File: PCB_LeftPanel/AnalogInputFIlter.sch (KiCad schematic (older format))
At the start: 24 parts, among them J24 Conn_01x03, J25 Conn_01x03, J26 Conn_01x03, J27 Conn_01x03, J28 Conn_01x03, J29 Conn_01x03, J30 Conn_01x03, J31 Conn_01x03

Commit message: Add files via upload
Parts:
- added J36: Conn_01x08_Male, Connector_PinHeader_2.54mm:PinHeader_1x08_P2.54mm_Vertical, symbol Connector:Conn_01x08_Male
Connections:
- net PA0: now also J36.1 (Pin_1)
- net PA1: now also J36.2 (Pin_2)
- net PA2: now also J36.3 (Pin_3)
- net PA3: now also J36.4 (Pin_4)
- net PA4: now also J36.5 (Pin_5)
- net PA5: now also J36.6 (Pin_6)
- net PA6: now also J36.7 (Pin_7)
- net PA7: now also J36.8 (Pin_8)
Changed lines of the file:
@@
 Wire Wire Line
 	6450 4700 6850 4700
+$Comp
+L Connector:Conn_01x08_Male J36
+U 1 1 616B3B5E
+P 2800 2000
+F 0 "J36" H 2908 2481 50  0000 C CNN
+F 1 "Conn_01x08_Male" H 2908 2390 50  0000 C CNN
+F 2 "Connector_PinHeader_2.54mm:PinHeader_1x08_P2.54mm_Vertical" H 2800 2000 50  0001 C CNN
+F 3 "~" H 2800 2000 50  0001 C CNN
+	1    2800 2000
+	1    0    0    -1
+$EndComp
+Wire Wire Line
+	3000 1700 5450 1700
+Connection ~ 5450 1700
+Wire Wire Line
+	3000 1800 4500 1800
+Wire Wire Line
+	4500 1800 4500 2200
+Wire Wire Line
+	4500 2200 5450 2200
+Connection ~ 5450 2200
+Wire Wire Line
+	3000 1900 4400 1900
+Wire Wire Line
+	4400 1900 4400 2700
+Wire Wire Line
+	4400 2700 5450 2700
+Connection ~ 5450 2700
+Wire Wire Line
+	3000 2000 4300 2000
+Wire Wire Line
+	4300 2000 4300 3200
+Wire Wire Line
+	4300 3200 5450 3200
+Connection ~ 5450 3200
+Wire Wire Line
+	5450 3700 4200 3700
+Wire Wire Line
+	4200 3700 4200 2100
+Wire Wire Line
+	4200 2100 3000 2100
+Connection ~ 5450 3700
+Wire Wire Line
+	3000 2200 4100 2200
+Wire Wire Line
+	4100 2200 4100 4200
+Wire Wire Line
+	4100 4200 5450 4200
+Connection ~ 5450 4200
+Wire Wire Line
+	5450 4700 4000 4700
+Wire Wire Line
+	4000 4700 4000 2300
+Wire Wire Line
+	4000 2300 3000 2300
+Connection ~ 5450 4700
+Wire Wire Line
+	3000 2400 3900 2400
+Wire Wire Line
+	3900 2400 3900 5200
+Wire Wire Line
+	3900 5200 5450 5200
+Connection ~ 5450 5200
 $EndSCHEMATC

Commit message: Add files via upload
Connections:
- net GND: now also C10.2, C11.2, C12.2, C13.2, C14.2, C15.2, C16.2, C3.2; no longer C10.1, C11.1, C12.1, C13.1, C14.1, C15.1, C16.1, C3.1
- net PA0: now also C3.1; no longer C3.2
- net PA1: now also C10.1; no longer C10.2
- net PA2: now also C11.1; no longer C11.2
- net PA3: now also C12.1; no longer C12.2
- net PA4: now also C13.1; no longer C13.2
- net PA5: now also C14.1; no longer C14.2
- net PA6: now also C15.1; no longer C15.2
- net PA7: now also C16.1; no longer C16.2
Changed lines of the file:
@@
 F 3 "~" H 6300 1700 50  0001 C CNN
 	1    6300 1700
-	0    1    1    0
+	0    -1   -1   0
 $EndComp
 $Comp
@@
 F 3 "~" H 6300 2200 50  0001 C CNN
 	1    6300 2200
-	0    1    1    0
+	0    -1   -1   0
 $EndComp
 $Comp
@@
 F 3 "~" H 6300 2700 50  0001 C CNN
 	1    6300 2700
-	0    1    1    0
+	0    -1   -1   0
 $EndComp
 $Comp
@@
 F 3 "~" H 6300 3200 50  0001 C CNN
 	1    6300 3200
-	0    1    1    0
+	0    -1   -1   0
 $EndComp
 $Comp
@@
 F 3 "~" H 6300 3700 50  0001 C CNN
 	1    6300 3700
-	0    1    1    0
+	0    -1   -1   0
 $EndComp
 $Comp
@@
 F 3 "~" H 6300 4200 50  0001 C CNN
 	1    6300 4200
-	0    1    1    0
+	0    -1   -1   0
 $EndComp
 $Comp
@@
 F 3 "~" H 6300 4700 50  0001 C CNN
 	1    6300 4700
-	0    1    1    0
+	0    -1   -1   0
 $EndComp
 $Comp
@@
 F 3 "~" H 6300 5200 50  0001 C CNN
 	1    6300 5200
-	0    1    1    0
+	0    -1   -1   0
 $EndComp
 Wire Wire Line

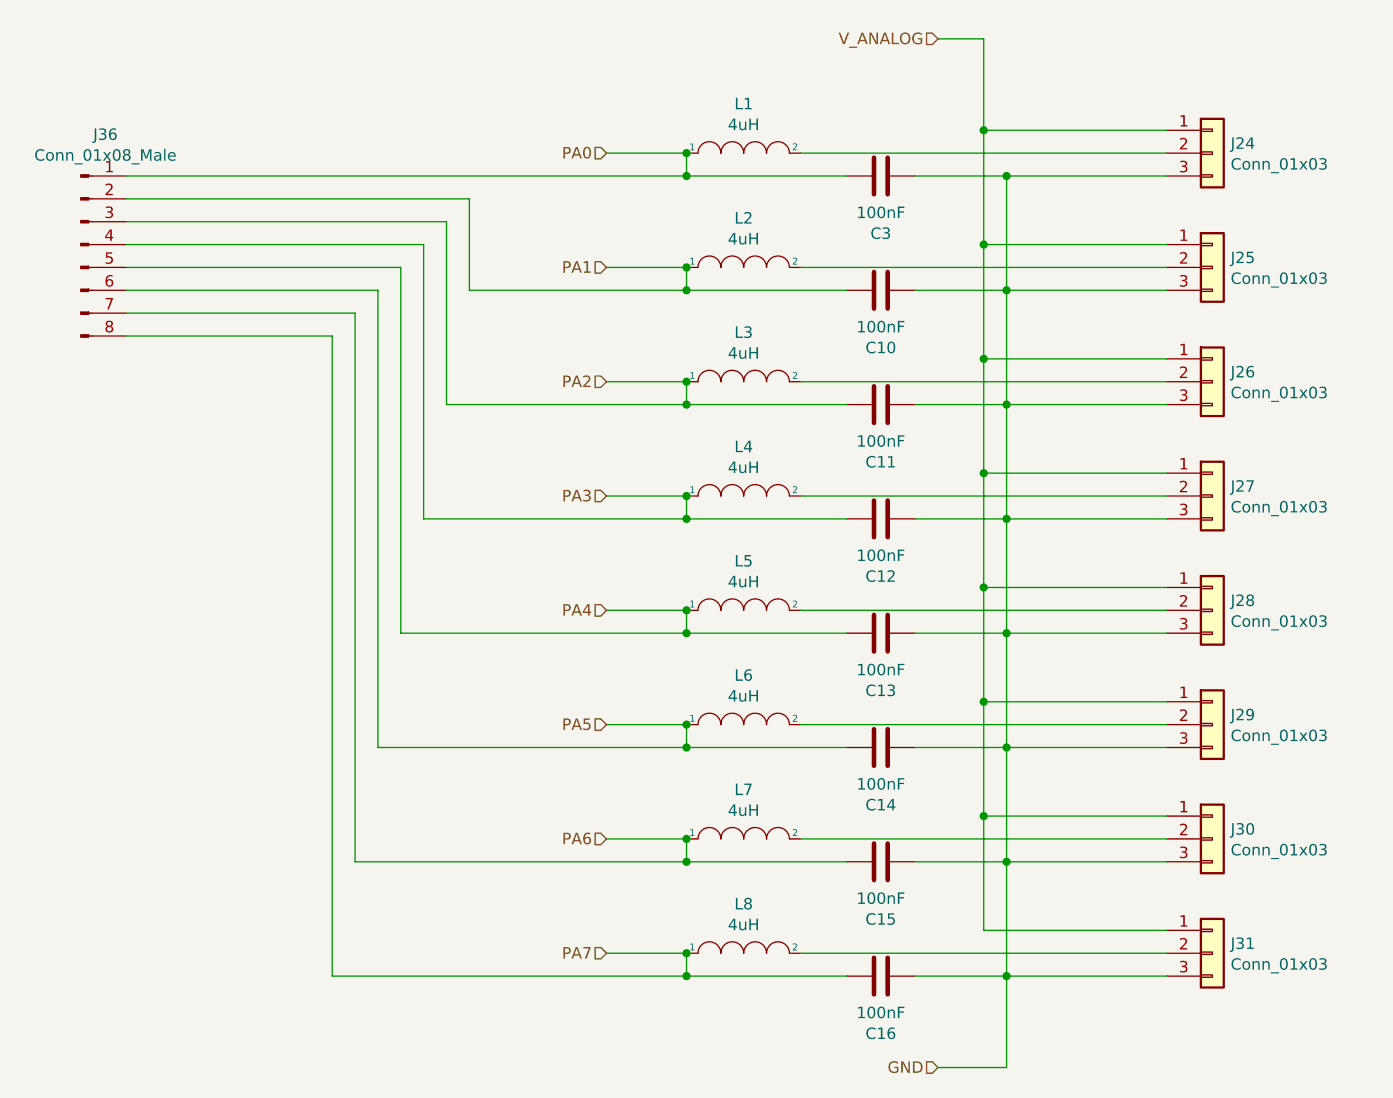
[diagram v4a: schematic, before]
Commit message: Add files via upload
Update to Revision 4.A
Board now based on Arduino Leonardo / Uno
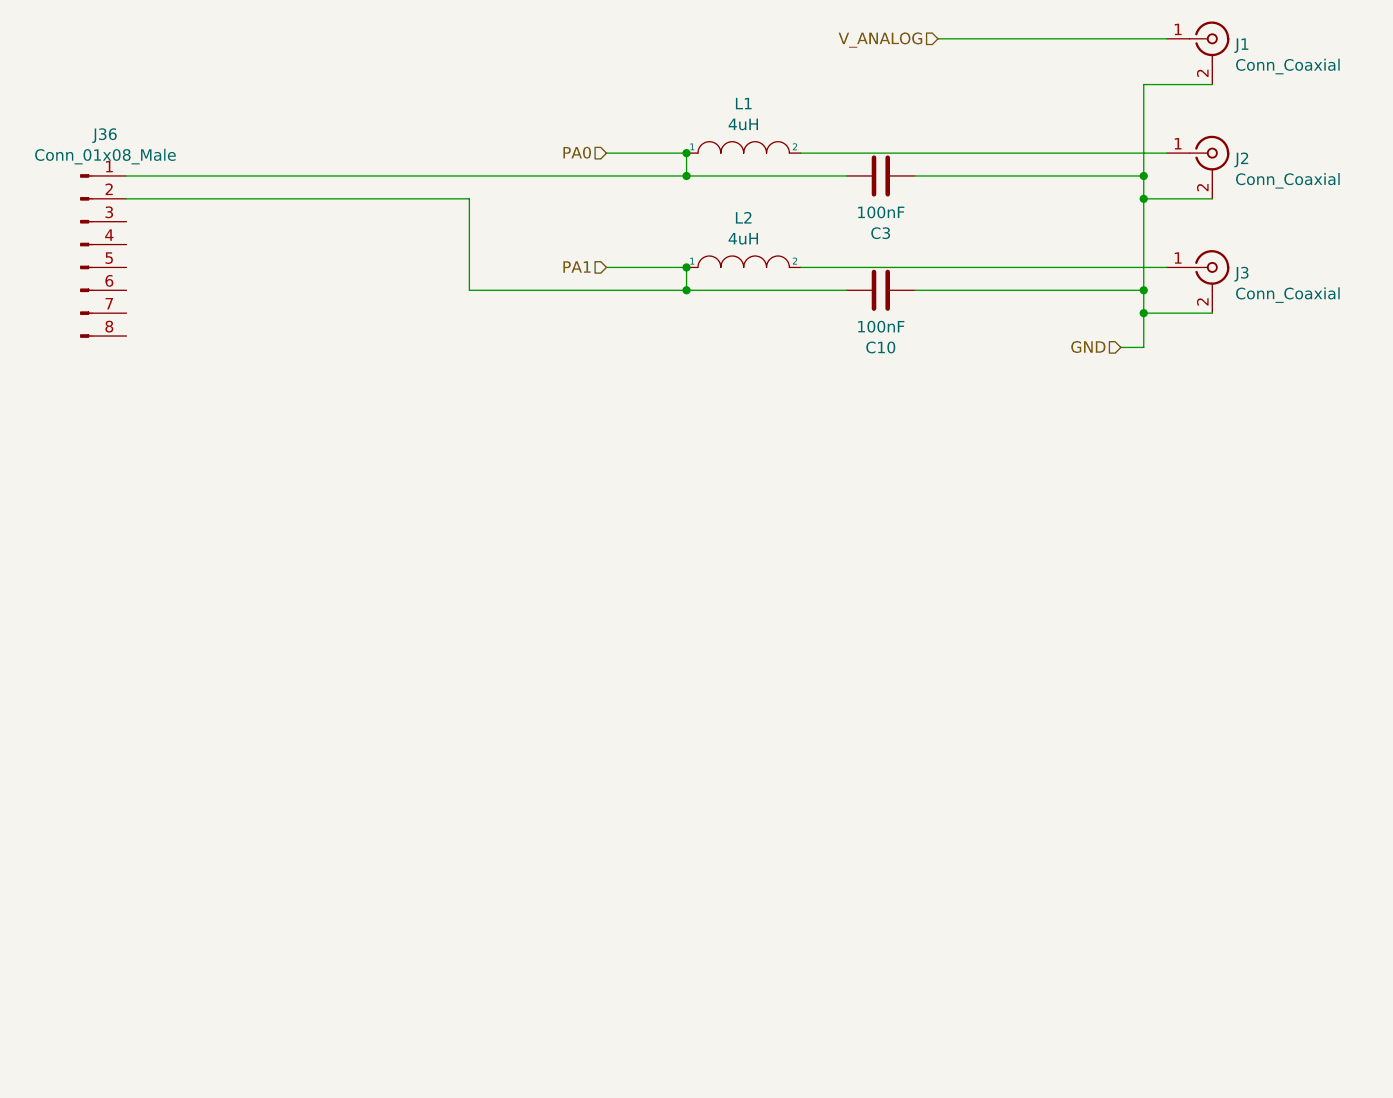
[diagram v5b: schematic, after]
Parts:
- removed C11, C12, C13, C14, C15, C16: 100nF, Capacitor_THT:CP_Radial_D8.0mm_P5.00mm, symbol Device:C
- removed J24, J25, J26, J27, J28, J29, J30, J31: Conn_01x03, Connector_PinHeader_2.54mm:PinHeader_1x03_P2.54mm_Vertical, symbol Connector_Generic:Conn_01x03
- removed L3, L4, L5, L6, L7, L8: 4uH, Inductor_THT:L_Axial_L5.0mm_D3.6mm_P10.00mm_Horizontal_Murata_BL01RN1A2A2, symbol pspice:INDUCTOR
- added J1, J2, J3: Conn_Coaxial, Connector_Coaxial:SMA_Amphenol_132203-12_Horizontal, symbol Connector:Conn_Coaxial
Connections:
- net GND: now also J1.2 (Ext), J2.2 (Ext), J3.2 (Ext)
- net V_ANALOG: now also J1.1 (In)
- net at L1.2: now also J2.1 (In)
- net at L2.2: now also J3.1 (In)
- net PA2: no longer names the net of J36.3 (Pin_3)
- net PA3: no longer names the net of J36.4 (Pin_4)
- net PA4: no longer names the net of J36.5 (Pin_5)
- net PA5: no longer names the net of J36.6 (Pin_6)
- net PA6: no longer names the net of J36.7 (Pin_7)
- net PA7: no longer names the net of J36.8 (Pin_8)
